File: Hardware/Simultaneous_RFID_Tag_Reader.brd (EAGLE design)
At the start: 77.5 x 53.3 mm, 37 parts, among them J2 FTDI, J3 JST, J4 U.FL, J5 Extra, J6 Screw Terminal, J7 GPIOs, U1 Nano, U2 TXB0104, U3 ESD Diode

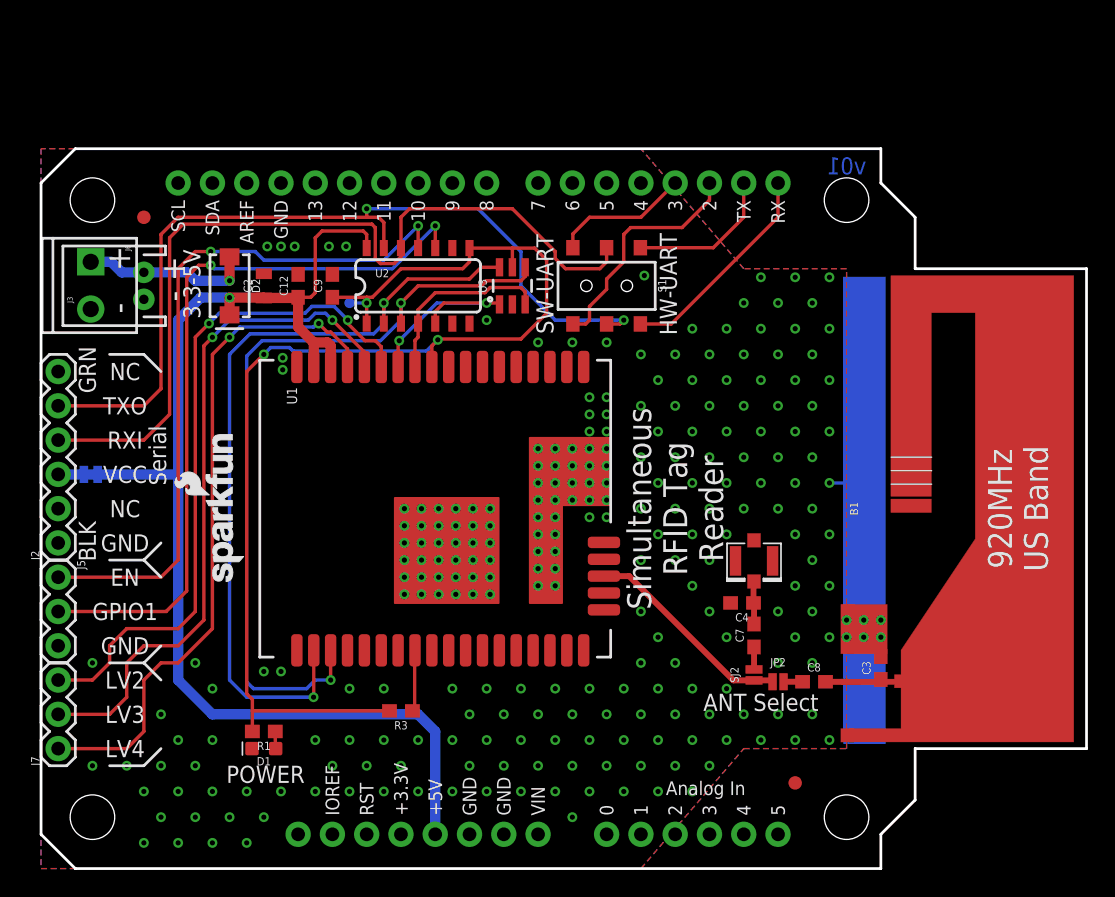
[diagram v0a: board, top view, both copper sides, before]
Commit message: Finalizing antenna. Adding buzzer.
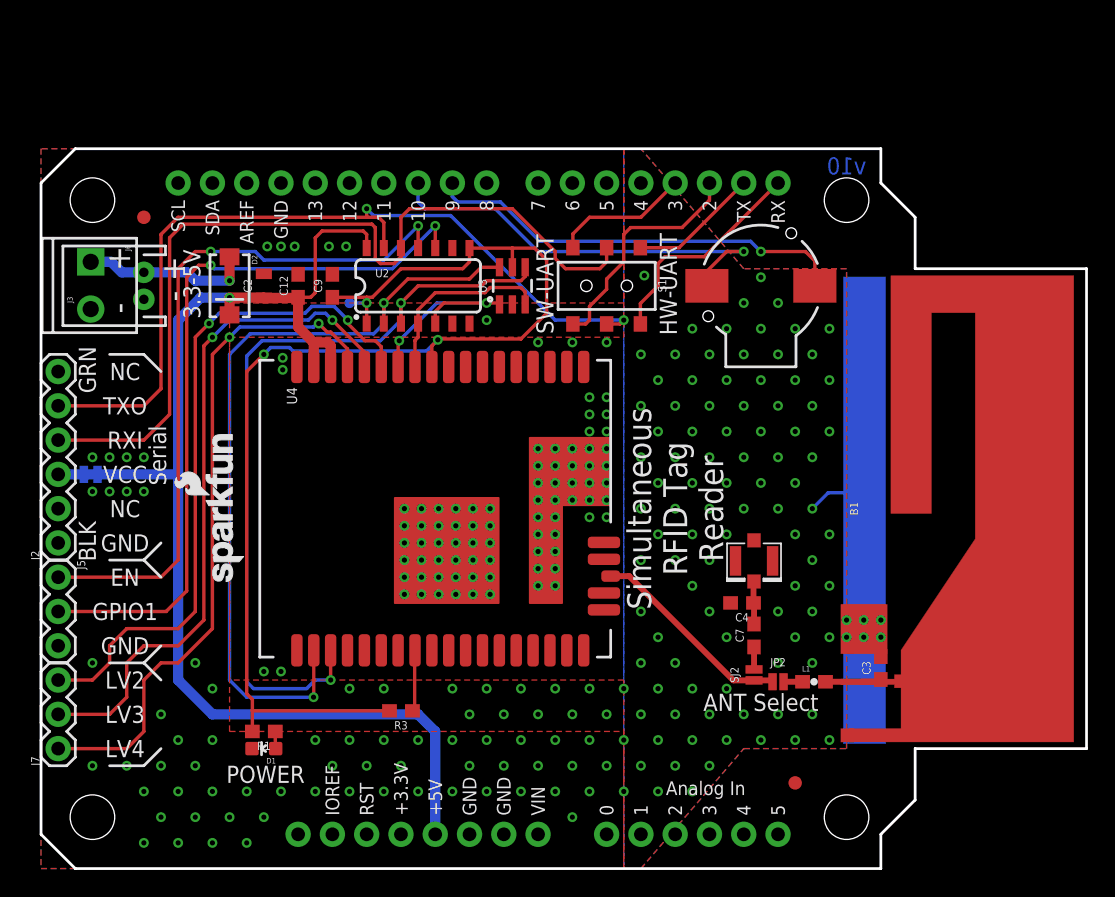
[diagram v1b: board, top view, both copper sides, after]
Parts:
- removed C8: ??, SparkFun-Capacitors:0603
- removed E2: Trace Antenna, UHF_RFID_Nano_Module:915MHZ_ANTENNA_TRIMBLE
- removed U1: Nano, UHF_RFID_Nano_Module:NANO_MODULE
- added E1: Trace Antenna, ThingMagic_Module:915MHZ_ANTENNA_TRIMBLE
- added L1: 3.9nH, ThingMagic_Module:0603
- added SG1: Buzzer, ThingMagic_Module:BUZZER-CCV
- added U4: Nano, ThingMagic_Module:NANO_MODULE
- C3, C4, C7: value ?? -> DNP
- D2: value 3A/40V/500mV -> B340A
- turned D1 to 90 degrees
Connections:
- new net N$11: B1.D9, SG1.+
- new net N$13: B1.D10, SG1.-
- net 3.3V: now also U4.10; no longer U1.10
- net ANT3: now also U4.39; no longer U1.39
- net ENABLE-LV: now also U4.11; no longer U1.11
- net GND: now also E1.GND@1, E1.GND@2, E1.GND@3, U4.1, U4.18, U4.19, U4.2, U4.29, U4.3, U4.30, U4.31, U4.32, U4.33, U4.34, U4.35, U4.36, U4.37, U4.38, U4.4, U4.40, U4.41, U4.5, U4.6, U4.7, U4.8, U4.9, U4.GND_PAD2; no longer E2.GND@1, E2.GND@2, E2.GND@3, U1.1, U1.18, U1.19, U1.2, U1.29, U1.3, U1.30, U1.31, U1.32, U1.33, U1.34, U1.35, U1.36, U1.37, U1.38, U1.4, U1.40, U1.41, U1.5, U1.6, U1.7, U1.8, U1.9, U1.GND_PAD2
- net GPIO1-LV: now also U4.12; no longer U1.12
- net GPIO2-LV: now also U4.13; no longer U1.13
- net GPIO3-LV: now also U4.14; no longer U1.14
- net GPIO4-LV: now also U4.15; no longer U1.15
- net N$1: now also E1.ANT, L1.2; no longer C8.2, E2.ANT
- net N$2: now also L1.1; no longer C8.1
- net N$4: now also U4.26; no longer U1.26
- net RXI-LV: now also U4.21; no longer U1.21
- net TXO-LV: now also U4.20; no longer U1.20
- net VCC: now also U4.16, U4.17; no longer U1.16, U1.17
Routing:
- net N$11: track 0.00 -> 31.7 mm, vias 0 -> 1
- net N$13: track 0.00 -> 31.5 mm, vias 0 -> 1
- net N$1: track 4.18 -> 5.73 mm
- net TXO: track 64.6 -> 63.2 mm
- net N$9: track 11.1 -> 9.65 mm
- net GND: track 9.69 -> 10.9 mm, vias 256 -> 260
- net ANT3: track 15.7 -> 15.2 mm
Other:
- board text added: "v10"
- board text removed: "920MHz US Band"
- board text removed: "v01"

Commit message: Added heat sink area and mounting holes.
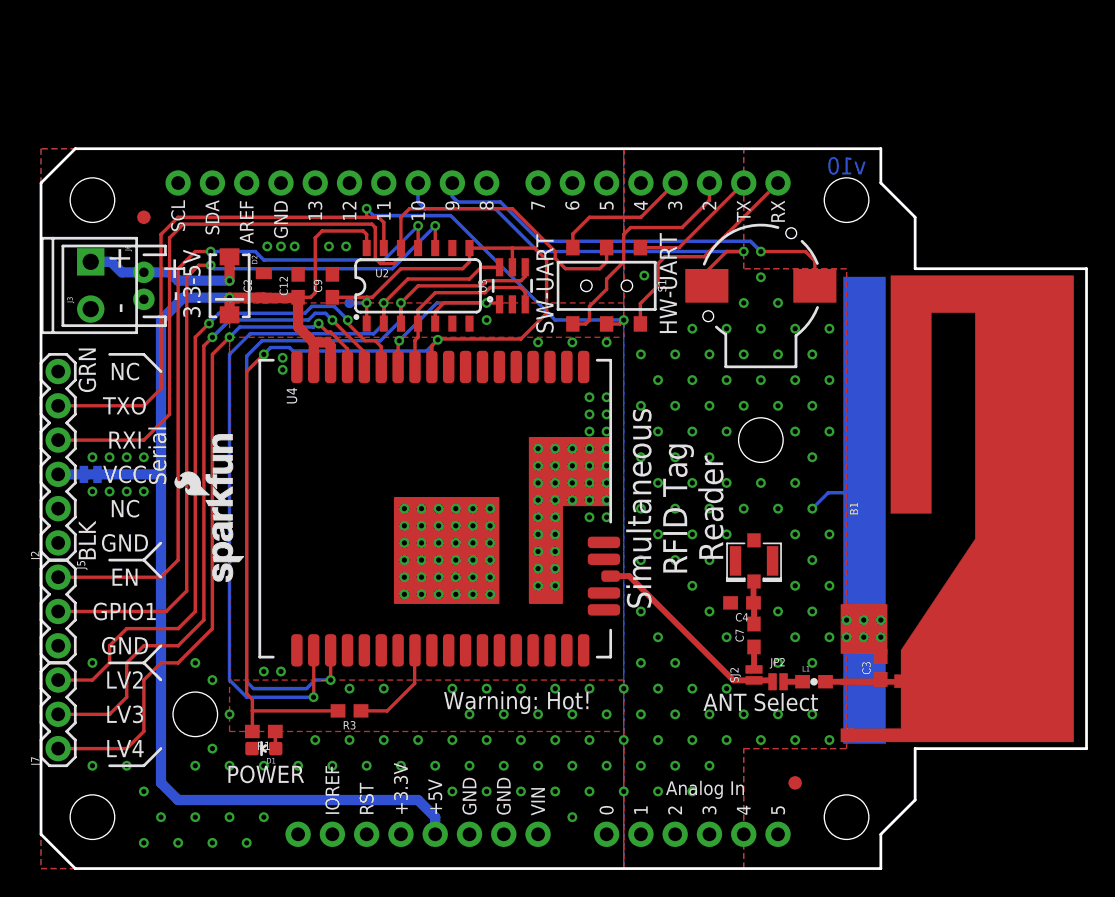
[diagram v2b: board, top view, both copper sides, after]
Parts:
- added STANDOFF5, STANDOFF6: STAND-OFF, SparkFun-Electromechanical:STAND-OFF
- moved LOGO3 57.8 mm to (67.7, 32.4), turned to 270 degrees
- moved R3 3.81 mm to (22.9, 11.7)
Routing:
- net 3.3V: track 90.4 -> 86.5 mm
- net N$4: track 4.56 -> 7.28 mm
- net VCC: track 91.0 -> 93.0 mm
- net GND: vias 260 -> 251
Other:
- board text added: "Warning: Hot!"

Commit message: Adding buzzer labels
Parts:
- C4, C7: value DNP -> TBD
- turned STANDOFF7 to 0 degrees
- turned STANDOFF8 to 0 degrees
- renumbered STANDOFF5 to STANDOFF8, STANDOFF6 to STANDOFF7
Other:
- board text added: "BZ1"
- board text added: "BZ2"
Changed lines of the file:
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@@
 <dimension x1="0" y1="0" x2="11.43" y2="11.43" x3="-3.81" y3="5.715" textsize="1.016" textratio="15" layer="47" dtype="vertical" unit="inch"/>
 <dimension x1="0" y1="0" x2="53.34" y2="31.75" x3="-11.43" y3="15.875" textsize="1.016" textratio="15" layer="47" dtype="vertical" unit="inch"/>
+<text x="30.48" y="47.244" size="1.27" layer="22" font="vector" ratio="15" rot="MR270" align="center">BZ1</text>
+<text x="27.94" y="47.244" size="1.27" layer="22" font="vector" ratio="15" rot="MR270" align="center">BZ2</text>
 </plain>
 <attributes>
@@
 <attribute name="PROD_ID" value="CAP-07879" x="62.23" y="14.859" size="1.778" layer="27" font="vector" ratio="15" rot="R90" display="off"/>
 </element>
-<element name="C4" library="SparkFun-Capacitors" package="0603" value="DNP" x="51.943" y="19.685" rot="R180">
+<element name="C4" library="SparkFun-Capacitors" package="0603" value="TBD" x="51.943" y="19.685" rot="R180">
 <attribute name="PROD_ID" value="CAP-07879" x="51.943" y="19.685" size="1.778" layer="27" font="vector" ratio="15" rot="R180" display="off"/>
 </element>
-<element name="C7" library="SparkFun-Capacitors" package="0603" value="DNP" x="52.832" y="17.272" rot="R90">
+<element name="C7" library="SparkFun-Capacitors" package="0603" value="TBD" x="52.832" y="17.272" rot="R90">
 <attribute name="PROD_ID" value="CAP-07879" x="52.832" y="17.272" size="1.778" layer="27" font="vector" ratio="15" rot="R90" display="off"/>
 </element>
@@
 <attribute name="PROD_ID" value="COMP-08568" x="53.34" y="43.18" size="1.778" layer="27" font="vector" ratio="15" display="off"/>
 </element>
-<element name="STANDOFF5" library="SparkFun-Electromechanical" package="STAND-OFF" value="STAND-OFF" x="53.34" y="31.75" smashed="yes" rot="R90"/>
-<element name="STANDOFF6" library="SparkFun-Electromechanical" package="STAND-OFF" value="STAND-OFF" x="11.43" y="11.43" smashed="yes" rot="R90"/>
+<element name="STANDOFF7" library="SparkFun-Electromechanical" package="STAND-OFF" value="STAND-OFF" x="11.43" y="11.43"/>
+<element name="STANDOFF8" library="SparkFun-Electromechanical" package="STAND-OFF" value="STAND-OFF" x="53.34" y="31.75"/>
 </elements>
 <signals>

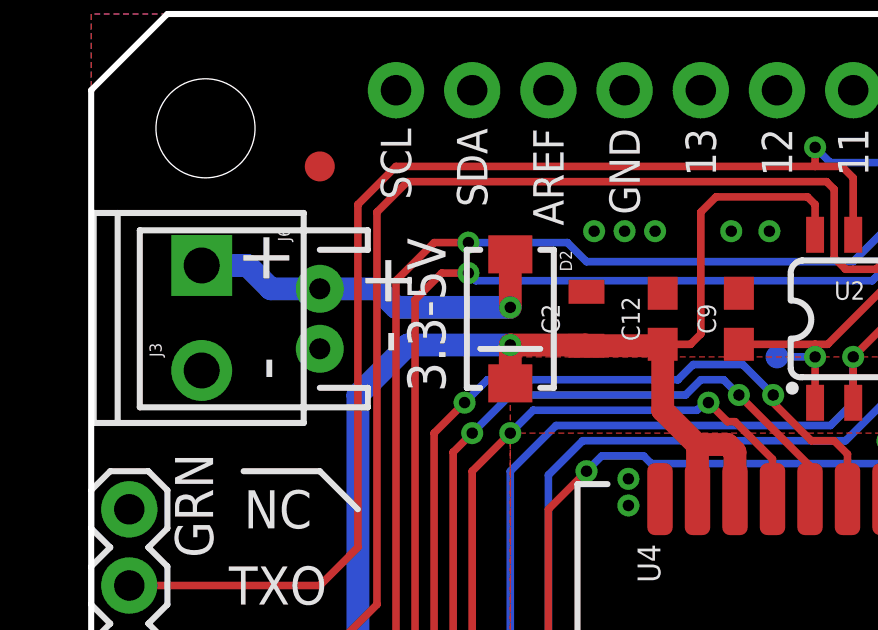
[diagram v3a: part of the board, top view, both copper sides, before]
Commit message: Changing input silk to 3.7-5V.
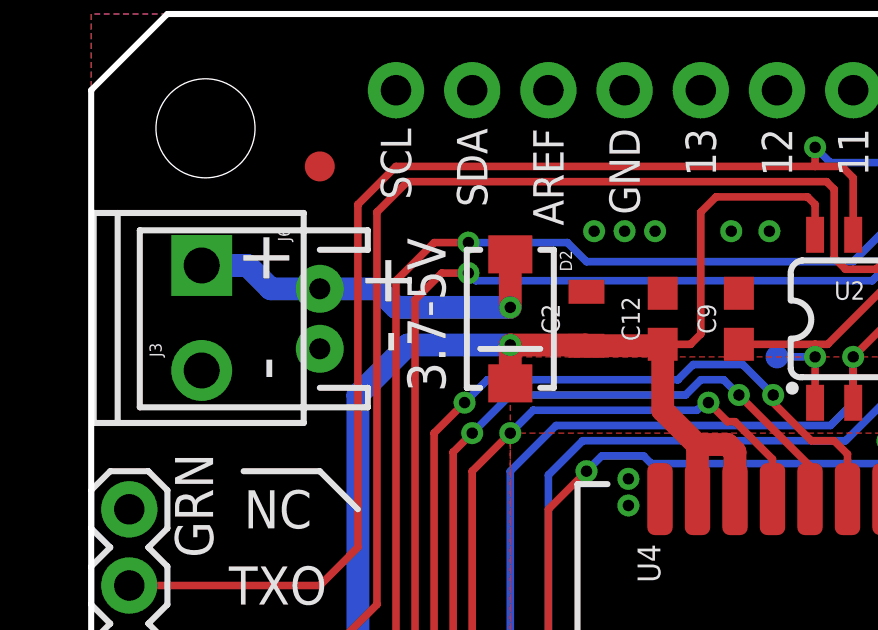
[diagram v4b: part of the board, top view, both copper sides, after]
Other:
- board text added: "3.7-5V"
- board text removed: "3.3-5V"
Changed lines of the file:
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@@
 <?xml version="1.0" encoding="utf-8"?>
 <!DOCTYPE eagle SYSTEM "eagle.dtd">
-<eagle version="7.6.0">
+<eagle version="7.5.0">
 <drawing>
 <settings>
@@
 <layer number="20" name="Dimension" color="15" fill="1" visible="yes" active="yes"/>
 <layer number="21" name="tPlace" color="16" fill="1" visible="yes" active="yes"/>
-<layer number="22" name="bPlace" color="14" fill="1" visible="no" active="yes"/>
+<layer number="22" name="bPlace" color="14" fill="1" visible="yes" active="yes"/>
 <layer number="23" name="tOrigins" color="15" fill="1" visible="yes" active="yes"/>
-<layer number="24" name="bOrigins" color="15" fill="1" visible="no" active="yes"/>
-<layer number="25" name="tNames" color="7" fill="1" visible="yes" active="yes"/>
+<layer number="24" name="bOrigins" color="15" fill="1" visible="yes" active="yes"/>
+<layer number="25" name="tNames" color="7" fill="1" visible="no" active="yes"/>
 <layer number="26" name="bNames" color="7" fill="1" visible="no" active="yes"/>
 <layer number="27" name="tValues" color="7" fill="1" visible="no" active="yes"/>
@@
 <layer number="43" name="vRestrict" color="2" fill="10" visible="no" active="yes"/>
 <layer number="44" name="Drills" color="7" fill="1" visible="no" active="yes"/>
-<layer number="45" name="Holes" color="7" fill="1" visible="no" active="yes"/>
+<layer number="45" name="Holes" color="7" fill="1" visible="yes" active="yes"/>
 <layer number="46" name="Milling" color="3" fill="1" visible="no" active="yes"/>
 <layer number="47" name="Measures" color="7" fill="1" visible="no" active="yes"/>
@@
 <layer number="49" name="Reference" color="7" fill="1" visible="no" active="yes"/>
 <layer number="50" name="dxf" color="7" fill="1" visible="no" active="no"/>
-<layer number="51" name="tDocu" color="6" fill="1" visible="no" active="yes"/>
+<layer number="51" name="tDocu" color="6" fill="1" visible="yes" active="yes"/>
 <layer number="52" name="bDocu" color="7" fill="1" visible="no" active="yes"/>
 <layer number="53" name="tGND_GNDA" color="7" fill="9" visible="no" active="no"/>
@@
 <dimension x1="0" y1="0" x2="52.832" y2="22.7965" x3="26.416" y3="-8.89" textsize="1.016" textratio="15" layer="47" dtype="horizontal" unit="inch"/>
 <dimension x1="77.47" y1="8.89" x2="77.47" y2="44.45" x3="85.09" y3="26.67" textsize="1.016" textratio="15" layer="47" dtype="vertical" unit="inch"/>
-<text x="11.176" y="43.307" size="1.27" layer="21" font="vector" ratio="15" rot="R270" align="center">3.3-5V</text>
-<text x="11.176" y="43.307" size="1.27" layer="22" font="vector" ratio="15" rot="MR270" align="center">3.3-5V</text>
+<text x="11.176" y="43.307" size="1.27" layer="21" font="vector" ratio="15" rot="R270" align="center">3.7-5V</text>
+<text x="11.176" y="43.307" size="1.27" layer="22" font="vector" ratio="15" rot="MR270" align="center">3.7-5V</text>
 <text x="72.39" y="26.543" size="1.778" layer="22" font="vector" ratio="15" rot="SMR270" align="center">Simultaneous
 RFID Tag

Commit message: Finishing matching network to u.FL
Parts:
- C4: value TBD -> DNP
- C7: value TBD -> 0.0
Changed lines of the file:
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@@
 <?xml version="1.0" encoding="utf-8"?>
 <!DOCTYPE eagle SYSTEM "eagle.dtd">
-<eagle version="7.5.0">
+<eagle version="7.2.0">
 <drawing>
 <settings>
@@
 <attribute name="PROD_ID" value="CAP-07879" x="62.23" y="14.859" size="1.778" layer="27" font="vector" ratio="15" rot="R90" display="off"/>
 </element>
-<element name="C4" library="SparkFun-Capacitors" package="0603" value="TBD" x="51.943" y="19.685" rot="R180">
+<element name="C4" library="SparkFun-Capacitors" package="0603" value="DNP" x="51.943" y="19.685" rot="R180">
 <attribute name="PROD_ID" value="CAP-07879" x="51.943" y="19.685" size="1.778" layer="27" font="vector" ratio="15" rot="R180" display="off"/>
 </element>
-<element name="C7" library="SparkFun-Capacitors" package="0603" value="TBD" x="52.832" y="17.272" rot="R90">
+<element name="C7" library="SparkFun-Capacitors" package="0603" value="0.0" x="52.832" y="17.272" rot="R90">
 <attribute name="PROD_ID" value="CAP-07879" x="52.832" y="17.272" size="1.778" layer="27" font="vector" ratio="15" rot="R90" display="off"/>
 </element>

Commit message: Adding cosmetic GND connection to schematic.
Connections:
- net GND: now also U4.GND_PAD1
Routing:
- net GND: track 10.9 -> 13.8 mm
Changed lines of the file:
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@@
 <?xml version="1.0" encoding="utf-8"?>
 <!DOCTYPE eagle SYSTEM "eagle.dtd">
-<eagle version="7.2.0">
+<eagle version="7.6.0">
 <drawing>
 <settings>
@@
 <setting verticaltext="up"/>
 </settings>
-<grid distance="0.05" unitdist="inch" unit="inch" style="lines" multiple="1" display="yes" altdistance="0.005" altunitdist="inch" altunit="inch"/>
+<grid distance="1" unitdist="mm" unit="mm" style="lines" multiple="1" display="yes" altdistance="0.1" altunitdist="mm" altunit="mm"/>
 <layers>
 <layer number="1" name="Top" color="4" fill="1" visible="yes" active="yes"/>
@@
 <layer number="47" name="Measures" color="7" fill="1" visible="no" active="yes"/>
 <layer number="48" name="Document" color="7" fill="1" visible="no" active="yes"/>
-<layer number="49" name="Reference" color="7" fill="1" visible="no" active="yes"/>
+<layer number="49" name="Reference" color="7" fill="1" visible="yes" active="yes"/>
 <layer number="50" name="dxf" color="7" fill="1" visible="no" active="no"/>
 <layer number="51" name="tDocu" color="6" fill="1" visible="yes" active="yes"/>
@@
 <via x="16.51" y="7.62" extent="1-16" drill="0.381"/>
 <via x="13.97" y="7.62" extent="1-16" drill="0.381"/>
+<contactref element="U4" pad="GND_PAD1"/>
+<wire x1="30.734" y1="24.13" x2="30.67" y2="24.13" width="0.254" layer="16"/>
+<wire x1="30.67" y1="24.13" x2="30.11" y2="23.57" width="0.254" layer="16"/>
+<wire x1="31.95" y1="24.05" x2="32" y2="24.1" width="0.254" layer="1"/>
+<wire x1="30.11" y1="23.57" x2="31.47" y2="23.57" width="0.254" layer="1"/>
+<wire x1="31.47" y1="23.57" x2="31.95" y2="24.05" width="0.254" layer="1"/>
+<wire x1="30.11" y1="23.57" x2="30.11" y2="23.57" width="0" layer="19" extent="1-16"/>
 </signal>
 <signal name="N$30">
